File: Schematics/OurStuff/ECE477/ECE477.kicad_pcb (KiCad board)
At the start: 2 copper layers, 105 x 40.5 mm, 62 parts, among them J1 USB_B_Micro, J2 Barrel_Jack, J3 OLED JST PH 7pin, J7 D30V30F3, Q1 SS8050-G, Q2 SS8050-G, U1 ESP32-WROOM-32E, U2 CP2102N-Axx-xQFN28, U3 USBLC6-2SC6

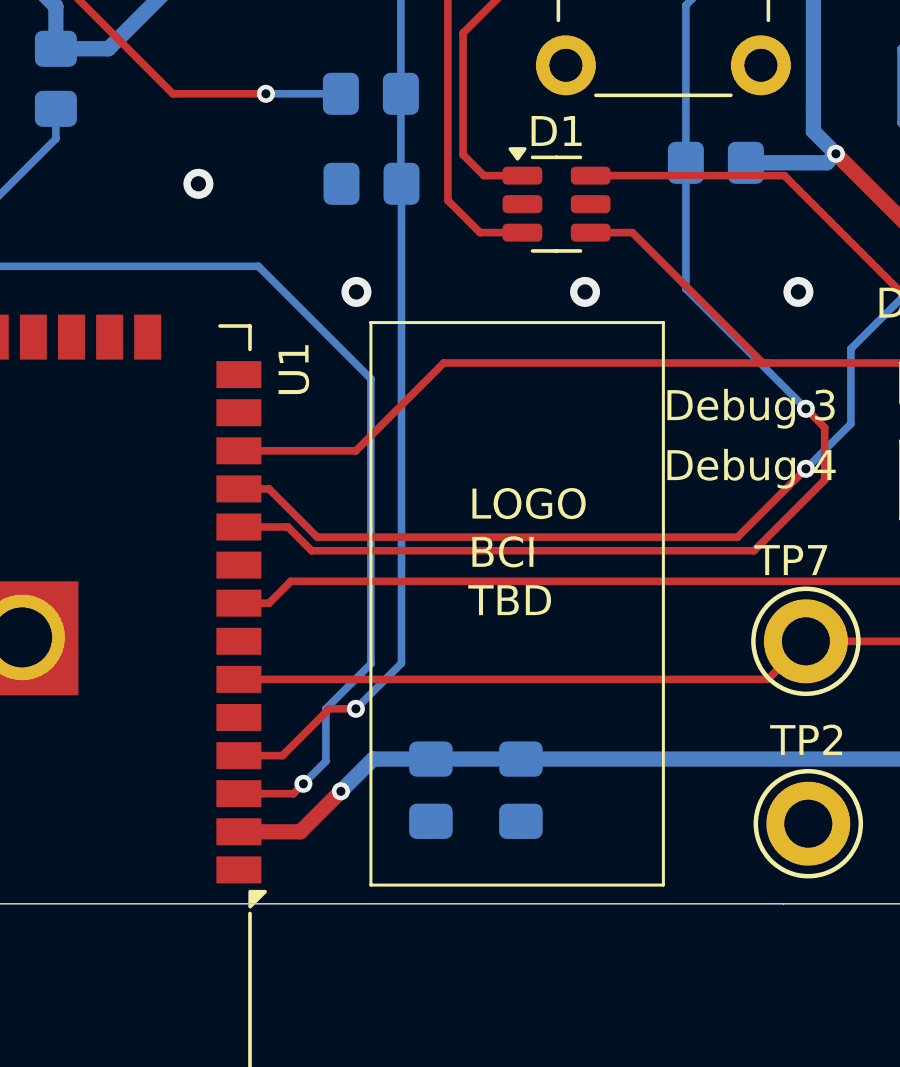
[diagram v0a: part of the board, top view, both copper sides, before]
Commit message: added bat mon capacitor
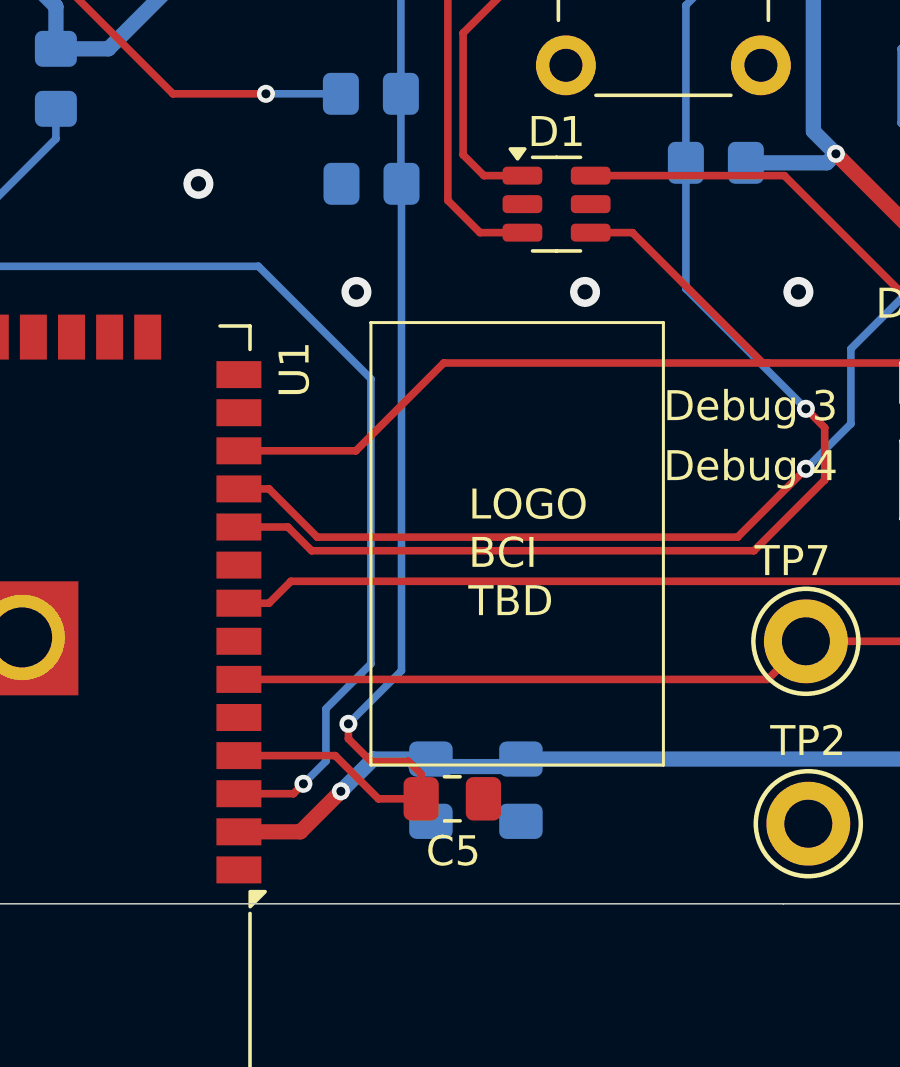
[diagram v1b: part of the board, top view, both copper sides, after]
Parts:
- added C5: 10uF, Capacitor_SMD:C_0805_2012Metric_Pad1.18x1.45mm_HandSolder, F.Cu at (179.0, 87.0)
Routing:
- net BAT_ADC: track 31.2 -> 38.1 mm

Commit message: added logo
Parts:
- added G***: LOGO, LOGO, F.Cu at (181.7, 77.7)
- moved TP5 1.12 mm to (176.2, 57.5)
- moved TP3 0.25 mm to (190.5, 53.2)
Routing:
- net BAT_ADC: track 38.1 -> 39.1 mm
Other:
- board text added: "Db-3"
- board text added: "Db-4"
- board text removed: "Debug 3"
- board text removed: "Debug 4"
- board text removed: "LOGO BCI TBD"

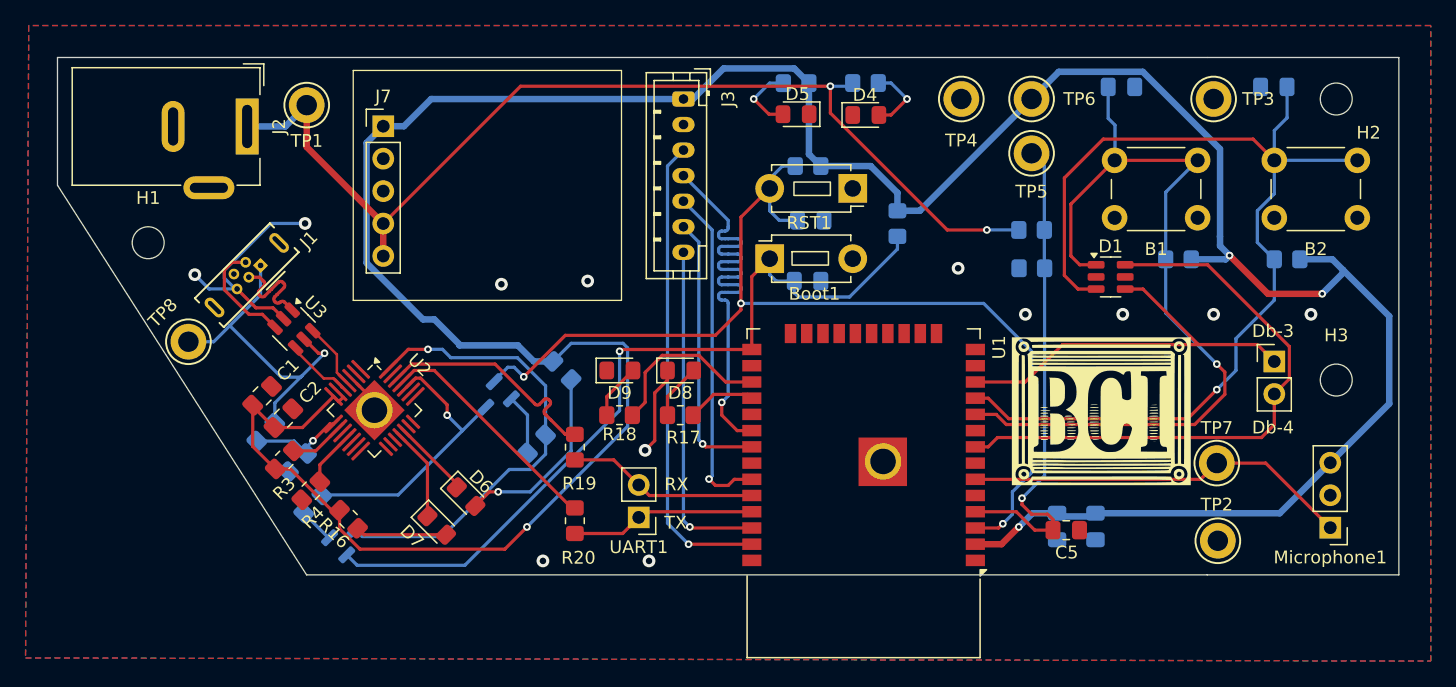
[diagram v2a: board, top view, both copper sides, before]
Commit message: added ferrite bead and fixed mic
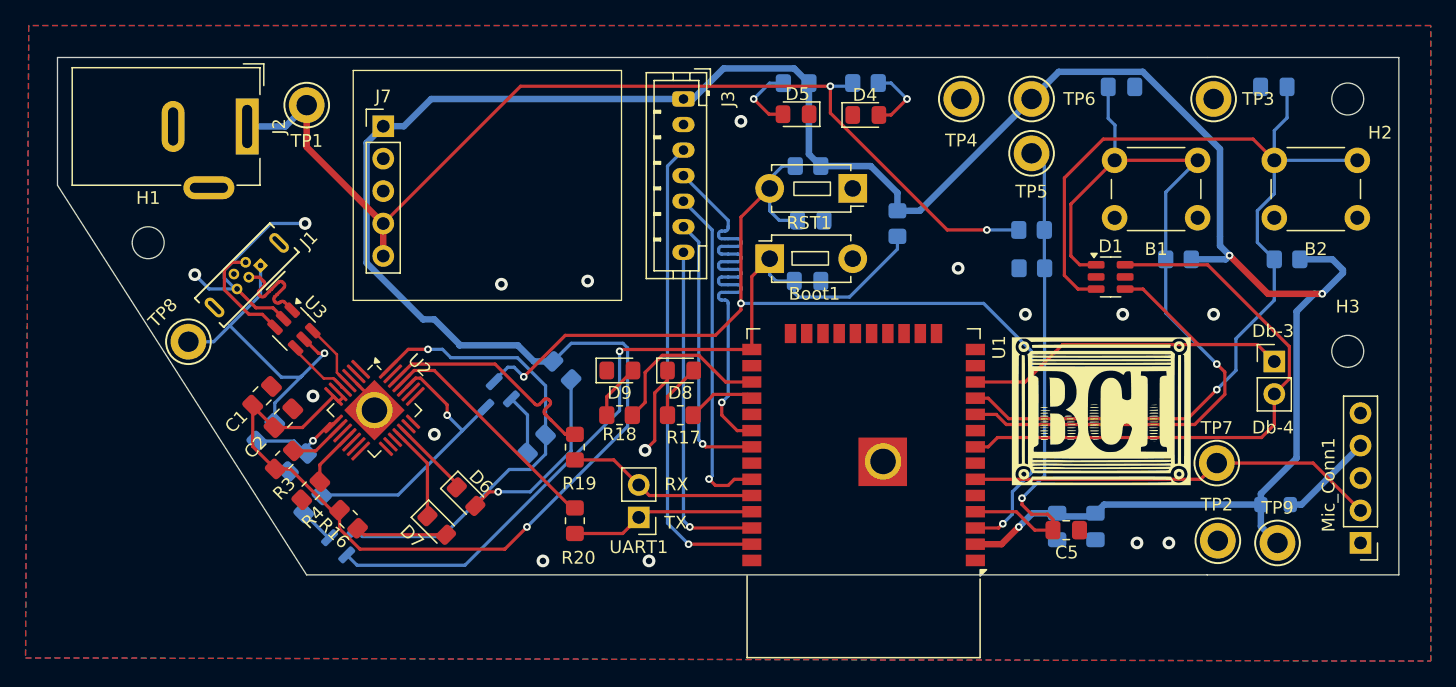
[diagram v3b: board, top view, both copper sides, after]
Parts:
- removed Microphone1: Microphone Connector, Connector_PinHeader_2.54mm:PinHeader_1x03_P2.54mm_Vertical
- added FB1: FerriteBead, Inductor_SMD:L_0805_2012Metric_Pad1.05x1.20mm_HandSolder, B.Cu at (195.3, 85.0)
- added Mic_Conn1: Conn_01x05_Socket, Connector_PinHeader_2.54mm:PinHeader_1x05_P2.54mm_Vertical, F.Cu at (202.0, 88.0)
- added TP9: Power, TestPoint:TestPoint_Keystone_5010-5014_Multipurpose, F.Cu at (195.5, 88.0)
- moved H3 2.42 mm to (201.0, 73.0)
- moved H2 0.90 mm to (201.0, 53.2)
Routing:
- net Vmic: track 0.00 -> 7.41 mm
- net +3.3V: track 250.3 -> 247.4 mm
- net /Mic_In: track 30.4 -> 32.2 mm
- net Gnd_Bat: vias 12 -> 16

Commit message: acute angle and added via
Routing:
- net Gnd_Bat: vias 16 -> 17
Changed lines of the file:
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@@
 		)
 		(property "Value" "Conn_01x05_Socket"
-			(at 0 12.49 360)
+			(at 0 12.49 0)
 			(layer "F.Fab")
 			(effects
@@
 		(tags "inductor handsolder")
 		(property "Reference" "FB1"
-			(at 0 1.55 360)
+			(at 0 1.55 0)
 			(layer "B.SilkS")
 			(effects
@@
 		)
 		(property "Value" "FerriteBead"
-			(at 0 -1.55 360)
+			(at 0 -1.55 0)
 			(layer "B.Fab")
 			(effects
@@
 		)
 		(fp_text user "${REFERENCE}"
-			(at 0 0 360)
+			(at 0 0 0)
 			(layer "B.Fab")
 			(effects
@@
 	)
 	(segment
-		(start 197.25 65.8)
-		(end 199.796 65.8)
-		(width 0.508)
-		(layer "B.Cu")
-		(net 1)
-	)
-	(segment
 		(start 136.75 86.75)
 		(end 144.627 78.873)
@@
 	)
 	(segment
+		(start 200.5 67)
+		(end 200.5 66.25)
+		(width 0.508)
+		(layer "B.Cu")
+		(net 1)
+	)
+	(segment
 		(start 149.75 53.25)
 		(end 152.144 50.856)
@@
 	)
 	(segment
-		(start 199.796 65.8)
-		(end 200.623 66.627)
-		(width 0.508)
-		(layer "B.Cu")
-		(net 1)
-	)
-	(segment
 		(start 165.75 62)
 		(end 167.5 62)
@@
 	)
 	(segment
+		(start 200.05 65.8)
+		(end 197.25 65.8)
+		(width 0.508)
+		(layer "B.Cu")
+		(net 1)
+	)
+	(segment
 		(start 124.196 56.684)
 		(end 125.5 55.38)
@@
 	)
 	(segment
-		(start 138.792892 73.792892)
-		(end 137.292892 73.792892)
+		(start 200.5 66.25)
+		(end 200.05 65.8)
 		(width 0.508)
 		(layer "B.Cu")
@@
 	)
 	(segment
-		(start 199 68.5)
-		(end 200.623 66.877)
+		(start 138.792892 73.792892)
+		(end 137.292892 73.792892)
 		(width 0.508)
 		(layer "B.Cu")
@@
 	)
 	(segment
+		(start 199 68.5)
+		(end 200.5 67)
+		(width 0.508)
+		(layer "B.Cu")
+		(net 1)
+	)
+	(segment
 		(start 184.961034 51.121)
 		(end 191 57.159966)
@@
 	)
 	(segment
-		(start 200.623 66.877)
-		(end 200.623 66.627)
-		(width 0.508)
-		(layer "B.Cu")
-		(net 1)
-	)
-	(segment
 		(start 129.5 70.5)
 		(end 128.615865 70.5)
@@
 		(size 1)
 		(drill 0.508)
+		(layers "F.Cu" "B.Cu")
+		(free yes)
+		(net 20)
+	)
+	(via
+		(at 185.5 67.25)
+		(size 1)
+		(drill 0.508)

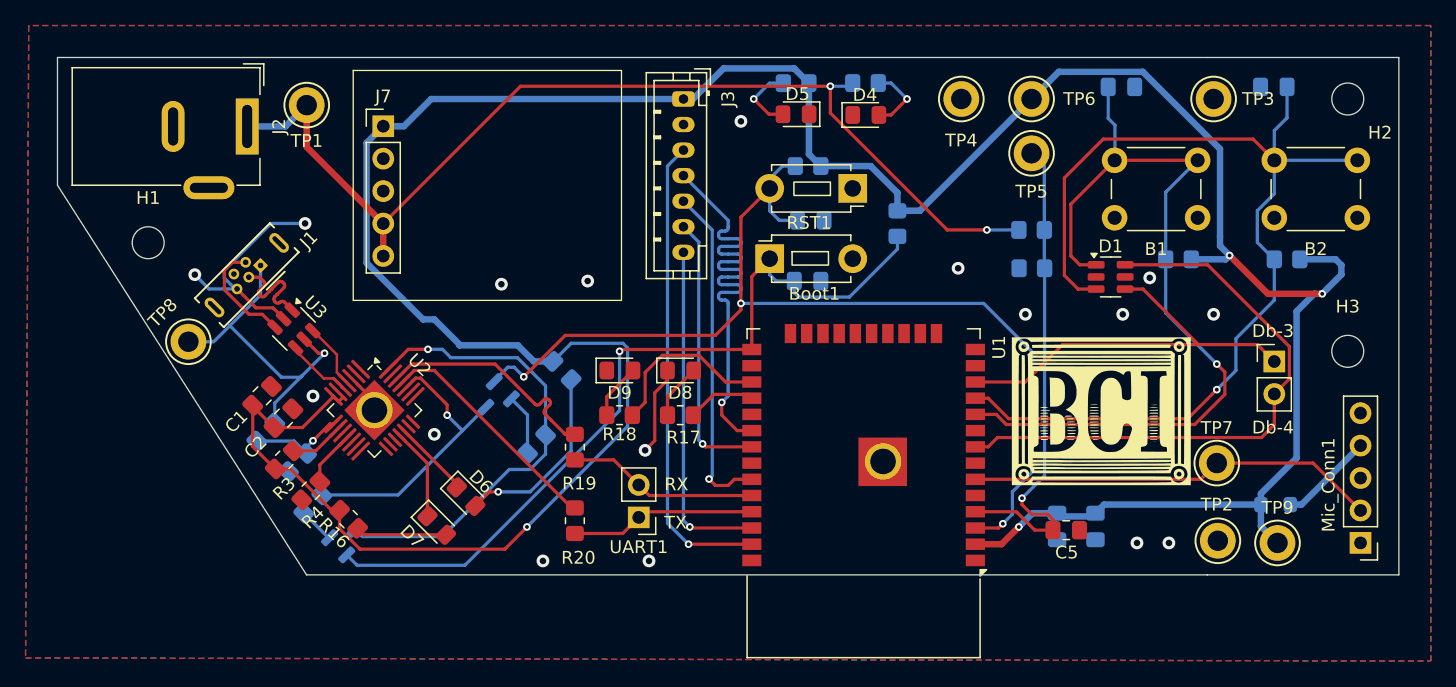
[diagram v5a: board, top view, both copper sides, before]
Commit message: updated PCB with suggestions 1-4
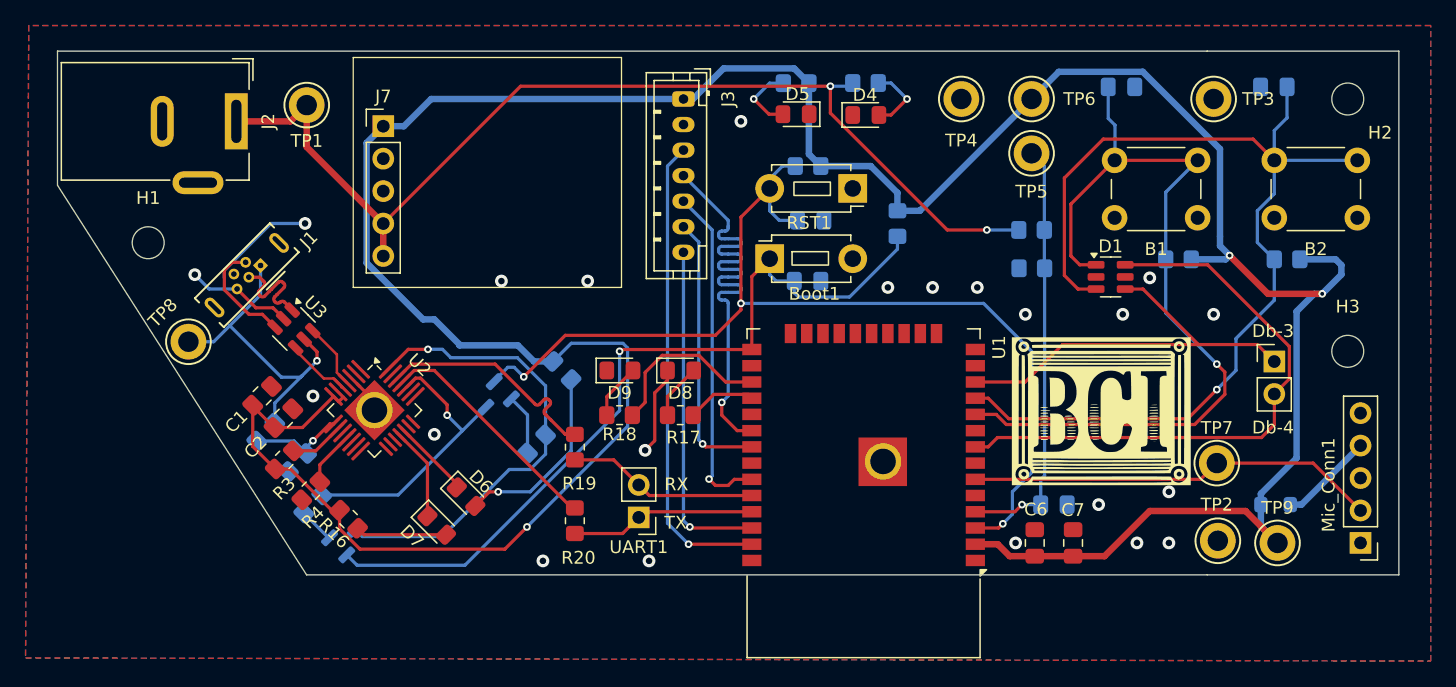
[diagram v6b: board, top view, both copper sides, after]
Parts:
- C5: moved to B.Cu
- C6, C7: moved to F.Cu
- R3: value 2k -> 1k
- moved C5 2.22 mm to (178.0, 85.0)
- moved C6 2.17 mm to (176.5, 88.0), turned to 90 degrees
- moved C7 2.17 mm to (179.5, 88.0), turned to 90 degrees
- moved J2 0.94 mm to (114.0, 55.0)
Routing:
- net BAT_ADC: track 39.1 -> 33.4 mm
- net +3.3V: track 247.4 -> 250.3 mm, vias 4 -> 3
- net Gnd_Bat: track 27.8 -> 26.6 mm, vias 17 -> 22
- net V_BUS: track 26.0 -> 25.2 mm
- net Vbat: track 81.6 -> 82.3 mm
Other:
- board size 105 x 40.5 mm -> 105 x 41 mm
